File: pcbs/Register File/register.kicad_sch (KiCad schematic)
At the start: 20 parts, among them U201 74HCT574, U203 74HC245

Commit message: More sketching
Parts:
- added D108 (x3): Blue, LED_SMD:LED_0603_1608Metric, symbol Device:LED
- added R809 (x3): 4k7, Resistor_SMD:R_0603_1608Metric, symbol Device:R
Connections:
- net ~{A_{Enable}}: now reaches U203.19 (CE)
- net ~{A_{Enable}}: now also D108.1 (K)
- net ~{B_{Enable}}: now reaches U203.19 (CE)
- net ~{B_{Enable}}: now also D108.1 (K)
- net ~{C_{Enable}}: now reaches U203.19 (CE)
- net ~{C_{Enable}}: now also D108.1 (K)
- new net: D108.2 (A), R809.1 (x3)
- new net +5V: R809.2, R809.2, R809.2

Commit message: More connecting
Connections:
- net GND: now also U201.1 (OE)
- net r1: now also D802.2 (A)
- net r2: now also D803.2 (A)
- net r3: now also D804.2 (A)
- net r4: now also D805.2 (A)
- net r5: now also D806.2 (A)
- net r6: now also D807.2 (A)
- net C_{write}: now reaches U201.11 (Cp)
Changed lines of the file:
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@@
+    (stroke (width 0) (type default))
+  )
+  (wire (pts (xy 43.18 124.46) (xy 50.8 124.46))
     (stroke (width 0) (type default))
   )
@@
     (stroke (width 0) (type default))
   )
+  (wire (pts (xy 43.18 114.3) (xy 50.8 114.3))
+    (stroke (width 0) (type default))
+  )
   (wire (pts (xy 208.28 85.09) (xy 226.06 85.09))
     (stroke (width 0) (type default))
@@
     (stroke (width 0) (type default))
   )
+  (wire (pts (xy 50.8 55.88) (xy 64.77 55.88))
+    (stroke (width 0) (type default))
+  )
+  (wire (pts (xy 43.18 104.14) (xy 50.8 104.14))
+    (stroke (width 0) (type default))
+  )
   (bus (pts (xy 228.6 92.71) (xy 228.6 95.25))
     (stroke (width 0) (type default))
@@
     (stroke (width 0) (type default))
   )
+  (wire (pts (xy 43.18 134.62) (xy 50.8 134.62))
+    (stroke (width 0) (type default))
+  )
   (bus (pts (xy 228.6 87.63) (xy 228.6 90.17))
     (stroke (width 0) (type default))
@@
     (stroke (width 0) (type default))
   )
+  (wire (pts (xy 64.77 58.42) (xy 60.96 58.42))
+    (stroke (width 0) (type default))
+  )
   (bus (pts (xy 228.6 132.08) (xy 228.6 134.62))
     (stroke (width 0) (type default))
@@
     (stroke (width 0) (type default))
   )
+  (wire (pts (xy 43.18 144.78) (xy 50.8 144.78))
+    (stroke (width 0) (type default))
+  )
   (wire (pts (xy 208.28 33.02) (xy 226.06 33.02))
     (stroke (width 0) (type default))
@@
     (stroke (width 0) (type default))
   )
+  (wire (pts (xy 43.18 154.94) (xy 50.8 154.94))
+    (stroke (width 0) (type default))
+  )
   (wire (pts (xy 182.88 127) (xy 120.65 127))
     (stroke (width 0) (type default))
   )
+  (wire (pts (xy 60.96 58.42) (xy 60.96 60.96))
+    (stroke (width 0) (type default))
+  )
   (bus (pts (xy 228.6 142.24) (xy 228.6 144.78))
     (stroke (width 0) (type default))
@@
     (effects (font (size 1.27 1.27)) (justify left bottom))
   )
+  (label "r1" (at 43.18 104.14 0) (fields_autoplaced)
+    (effects (font (size 1.27 1.27)) (justify left bottom))
+  )
+  (label "r5" (at 43.18 144.78 0) (fields_autoplaced)
+    (effects (font (size 1.27 1.27)) (justify left bottom))
+  )
+  (label "r2" (at 43.18 114.3 0) (fields_autoplaced)
+    (effects (font (size 1.27 1.27)) (justify left bottom))
+  )
   (label "C7" (at 50.8 50.8 0) (fields_autoplaced)
     (effects (font (size 1.27 1.27)) (justify left bottom))
@@
     (effects (font (size 1.27 1.27)) (justify left bottom))
   )
+  (label "r3" (at 43.18 124.46 0) (fields_autoplaced)
+    (effects (font (size 1.27 1.27)) (justify left bottom))
+  )
   (label "r5" (at 99.06 45.72 0) (fields_autoplaced)
     (effects (font (size 1.27 1.27)) (justify left bottom))
@@
     (effects (font (size 1.27 1.27)) (justify left bottom))
   )
+  (label "r6" (at 43.18 154.94 0) (fields_autoplaced)
+    (effects (font (size 1.27 1.27)) (justify left bottom))
+  )
   (label "B2" (at 208.28 85.09 0) (fields_autoplaced)
     (effects (font (size 1.27 1.27)) (justify left bottom))
@@
   )
   (label "r0" (at 43.18 93.98 0) (fields_autoplaced)
+    (effects (font (size 1.27 1.27)) (justify left bottom))
+  )
+  (label "r4" (at 43.18 134.62 0) (fields_autoplaced)
     (effects (font (size 1.27 1.27)) (justify left bottom))
   )
@@
   (hierarchical_label "B[0..7]" (shape output) (at 247.65 72.39 0) (fields_autoplaced)
     (effects (font (size 1.27 1.27)) (justify left))
+  )
+  (hierarchical_label "C_{write}" (shape input) (at 50.8 55.88 180) (fields_autoplaced)
+    (effects (font (size 1.27 1.27)) (justify right))
   )
   (symbol (lib_id "Device:R") (at 166.37 116.84 270) (unit 1)
@@
         )
       )
+    )
+  )
+  (symbol (lib_name "GND_1") (lib_id "power:GND") (at 60.96 60.96 0) (unit 1)
+    (in_bom yes) (on_board yes) (dnp no) (fields_autoplaced)
+    (property "Reference" "#PWR0205" (at 60.96 67.31 0)
+      (effects (font (size 1.27 1.27)) hide)
+    )
+    (property "Value" "GND" (at 60.96 66.04 0)
+      (effects (font (size 1.27 1.27)))
+    )
+    (property "Footprint" "" (at 60.96 60.96 0)
+      (effects (font (size 1.27 1.27)) hide)
+    )
+    (property "Datasheet" "" (at 60.96 60.96 0)
+      (effects (font (size 1.27 1.27)) hide)
+    )
+    (pin "1")
+    (instances
+      (project "Register File"
+        (path "/9748b4de-07f7-464d-8b11-64fc866bac4c/9394d714-1820-477b-aab0-a9d71bb5ee5c"
+          (reference "#PWR0205") (unit 1)
+        )
+        (path "/9748b4de-07f7-464d-8b11-64fc866bac4c/834893a6-a9c4-4230-b12d-8490f053213e"
+          (reference "#PWR0305") (unit 1)
+        )
+        (path "/9748b4de-07f7-464d-8b11-64fc866bac4c/4dbf28be-5b5c-4207-8488-535f1c399bc6"
+          (reference "#PWR0405") (unit 1)
+        )
+        (path "/9748b4de-07f7-464d-8b11-64fc866bac4c/cb795ff7-ba35-4df7-ae01-85f6e0183a53"
+          (reference "#PWR0505") (unit 1)
+        )
+        (path "/9748b4de-07f7-464d-8b11-64fc866bac4c/c5b4a55a-958e-4012-8139-b0afd70d67a1"
+          (reference "#PWR0605") (unit 1)
+        )
+        (path "/9748b4de-07f7-464d-8b11-64fc866bac4c/a37b855b-764b-47a1-be98-45e29ef72f3b"
+          (reference "#PWR0705") (unit 1)
+        )
+        (path "/9748b4de-07f7-464d-8b11-64fc866bac4c/b38b4b23-22e0-4015-98d9-f235dafba938"
+          (reference "#PWR0805") (unit 1)
+        )
+        (path "/9748b4de-07f7-464d-8b11-64fc866bac4c/5f8f38cf-62d2-470f-8060-72fd5c305ae9"
+          (reference "#PWR0905") (unit 1)
+        )
+      )

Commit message: More work
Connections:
- net +5V: now also U201.20 (VCC), U203.20 (VCC), U203.20 (VCC), U203.20 (VCC)
- net GND: now also U201.10 (GND), U203.10 (GND), U203.10 (GND), U203.10 (GND)

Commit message: Remember the control buses...
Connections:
- net +5V: now also U203.1 (A->B), U203.1 (A->B), U203.1 (A->B)
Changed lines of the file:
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@@
+    (stroke (width 0) (type default))
+  )
+  (wire (pts (xy 176.53 149.86) (xy 182.88 149.86))
     (stroke (width 0) (type default))
   )
@@
     (stroke (width 0) (type default))
   )
+  (wire (pts (xy 176.53 102.87) (xy 182.88 102.87))
+    (stroke (width 0) (type default))
+  )
   (wire (pts (xy 208.28 87.63) (xy 226.06 87.63))
     (stroke (width 0) (type default))
@@
   )
   (wire (pts (xy 76.2 154.94) (xy 76.2 144.78))
+    (stroke (width 0) (type default))
+  )
+  (wire (pts (xy 176.53 55.88) (xy 182.88 55.88))
     (stroke (width 0) (type default))
   )
@@
     )
   )
+  (symbol (lib_id "power:+5V") (at 176.53 102.87 90) (unit 1)
+    (in_bom yes) (on_board yes) (dnp no) (fields_autoplaced)
+    (property "Reference" "#PWR0315" (at 180.34 102.87 0)
+      (effects (font (size 1.27 1.27)) hide)
+    )
+    (property "Value" "+5V" (at 172.72 102.87 90)
+      (effects (font (size 1.27 1.27)) (justify left))
+    )
+    (property "Footprint" "" (at 176.53 102.87 0)
+      (effects (font (size 1.27 1.27)) hide)
+    )
+    (property "Datasheet" "" (at 176.53 102.87 0)
+      (effects (font (size 1.27 1.27)) hide)
+    )
+    (pin "1")
+    (instances
+      (project "Register File"
+        (path "/9748b4de-07f7-464d-8b11-64fc866bac4c/834893a6-a9c4-4230-b12d-8490f053213e"
+          (reference "#PWR0315") (unit 1)
+        )
+        (path "/9748b4de-07f7-464d-8b11-64fc866bac4c/9394d714-1820-477b-aab0-a9d71bb5ee5c"
+          (reference "#PWR0215") (unit 1)
+        )
+        (path "/9748b4de-07f7-464d-8b11-64fc866bac4c/4dbf28be-5b5c-4207-8488-535f1c399bc6"
+          (reference "#PWR0415") (unit 1)
+        )
+        (path "/9748b4de-07f7-464d-8b11-64fc866bac4c/cb795ff7-ba35-4df7-ae01-85f6e0183a53"
+          (reference "#PWR0515") (unit 1)
+        )
+        (path "/9748b4de-07f7-464d-8b11-64fc866bac4c/c5b4a55a-958e-4012-8139-b0afd70d67a1"
+          (reference "#PWR0615") (unit 1)
+        )
+        (path "/9748b4de-07f7-464d-8b11-64fc866bac4c/a37b855b-764b-47a1-be98-45e29ef72f3b"
+          (reference "#PWR0715") (unit 1)
+        )
+        (path "/9748b4de-07f7-464d-8b11-64fc866bac4c/b38b4b23-22e0-4015-98d9-f235dafba938"
+          (reference "#PWR0815") (unit 1)
+        )
+        (path "/9748b4de-07f7-464d-8b11-64fc866bac4c/5f8f38cf-62d2-470f-8060-72fd5c305ae9"
+          (reference "#PWR0915") (unit 1)
+        )
+      )
+    )
+  )
   (symbol (lib_id "Device:LED") (at 54.61 144.78 180) (unit 1)
     (in_bom yes) (on_board yes) (dnp no) (fields_autoplaced)
@@
         (path "/9748b4de-07f7-464d-8b11-64fc866bac4c/5f8f38cf-62d2-470f-8060-72fd5c305ae9"
           (reference "R906") (unit 1)
+        )
+      )
+    )
+  )
+  (symbol (lib_id "power:+5V") (at 176.53 149.86 90) (unit 1)
+    (in_bom yes) (on_board yes) (dnp no) (fields_autoplaced)
+    (property "Reference" "#PWR0316" (at 180.34 149.86 0)
+      (effects (font (size 1.27 1.27)) hide)
+    )
+    (property "Value" "+5V" (at 172.72 149.86 90)
+      (effects (font (size 1.27 1.27)) (justify left))
+    )
+    (property "Footprint" "" (at 176.53 149.86 0)
+      (effects (font (size 1.27 1.27)) hide)
+    )
+    (property "Datasheet" "" (at 176.53 149.86 0)
+      (effects (font (size 1.27 1.27)) hide)
+    )
+    (pin "1")
+    (instances
+      (project "Register File"
+        (path "/9748b4de-07f7-464d-8b11-64fc866bac4c/834893a6-a9c4-4230-b12d-8490f053213e"
+          (reference "#PWR0316") (unit 1)
+        )
+        (path "/9748b4de-07f7-464d-8b11-64fc866bac4c/9394d714-1820-477b-aab0-a9d71bb5ee5c"
+          (reference "#PWR0216") (unit 1)
+        )
+        (path "/9748b4de-07f7-464d-8b11-64fc866bac4c/4dbf28be-5b5c-4207-8488-535f1c399bc6"
+          (reference "#PWR0416") (unit 1)
+        )
+        (path "/9748b4de-07f7-464d-8b11-64fc866bac4c/cb795ff7-ba35-4df7-ae01-85f6e0183a53"
+          (reference "#PWR0516") (unit 1)
+        )
+        (path "/9748b4de-07f7-464d-8b11-64fc866bac4c/c5b4a55a-958e-4012-8139-b0afd70d67a1"
+          (reference "#PWR0616") (unit 1)
+        )
+        (path "/9748b4de-07f7-464d-8b11-64fc866bac4c/a37b855b-764b-47a1-be98-45e29ef72f3b"
+          (reference "#PWR0716") (unit 1)
+        )
+        (path "/9748b4de-07f7-464d-8b11-64fc866bac4c/b38b4b23-22e0-4015-98d9-f235dafba938"
+          (reference "#PWR0816") (unit 1)
+        )
+        (path "/9748b4de-07f7-464d-8b11-64fc866bac4c/5f8f38cf-62d2-470f-8060-72fd5c305ae9"
+          (reference "#PWR0916") (unit 1)
         )
       )
@@
         )
       )
+    )
+  )
+  (symbol (lib_id "power:+5V") (at 176.53 55.88 90) (unit 1)
+    (in_bom yes) (on_board yes) (dnp no) (fields_autoplaced)
+    (property "Reference" "#PWR0314" (at 180.34 55.88 0)
+      (effects (font (size 1.27 1.27)) hide)
+    )
+    (property "Value" "+5V" (at 172.72 55.88 90)
+      (effects (font (size 1.27 1.27)) (justify left))
+    )
+    (property "Footprint" "" (at 176.53 55.88 0)
+      (effects (font (size 1.27 1.27)) hide)
+    )
+    (property "Datasheet" "" (at 176.53 55.88 0)
+      (effects (font (size 1.27 1.27)) hide)
+    )
+    (pin "1")
+    (instances
+      (project "Register File"
+        (path "/9748b4de-07f7-464d-8b11-64fc866bac4c/834893a6-a9c4-4230-b12d-8490f053213e"
+          (reference "#PWR0314") (unit 1)
+        )
+        (path "/9748b4de-07f7-464d-8b11-64fc866bac4c/9394d714-1820-477b-aab0-a9d71bb5ee5c"
+          (reference "#PWR0214") (unit 1)
+        )
+        (path "/9748b4de-07f7-464d-8b11-64fc866bac4c/4dbf28be-5b5c-4207-8488-535f1c399bc6"
+          (reference "#PWR0414") (unit 1)
+        )
+        (path "/9748b4de-07f7-464d-8b11-64fc866bac4c/cb795ff7-ba35-4df7-ae01-85f6e0183a53"
+          (reference "#PWR0514") (unit 1)
+        )
+        (path "/9748b4de-07f7-464d-8b11-64fc866bac4c/c5b4a55a-958e-4012-8139-b0afd70d67a1"
+          (reference "#PWR0614") (unit 1)
+        )
+        (path "/9748b4de-07f7-464d-8b11-64fc866bac4c/a37b855b-764b-47a1-be98-45e29ef72f3b"
+          (reference "#PWR0714") (unit 1)
+        )
+        (path "/9748b4de-07f7-464d-8b11-64fc866bac4c/b38b4b23-22e0-4015-98d9-f235dafba938"
+          (reference "#PWR0814") (unit 1)
+        )
+        (path "/9748b4de-07f7-464d-8b11-64fc866bac4c/5f8f38cf-62d2-470f-8060-72fd5c305ae9"
+          (reference "#PWR0914") (unit 1)
+        )
+      )

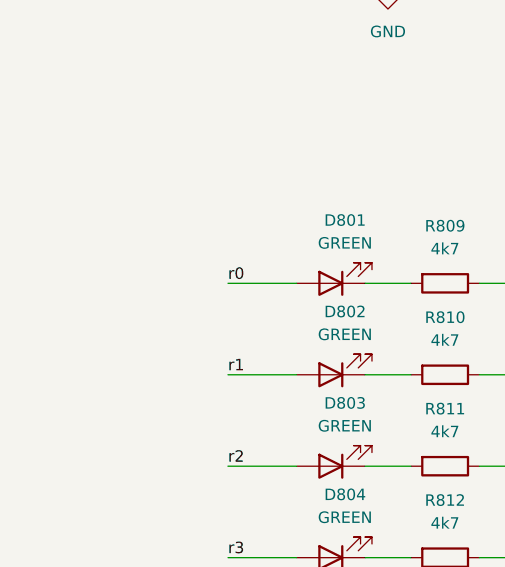
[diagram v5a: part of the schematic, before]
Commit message: Adding some capacitors
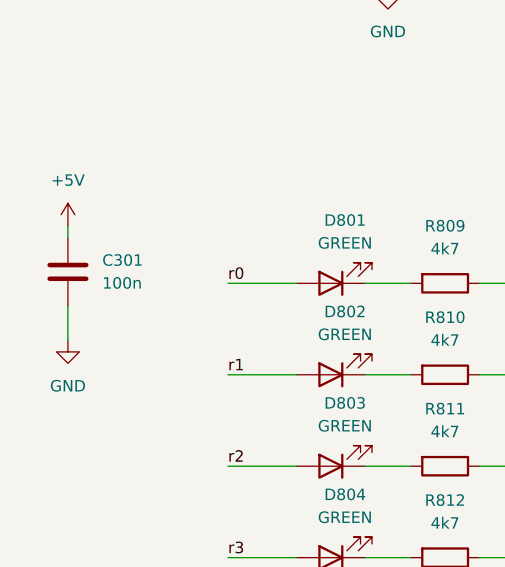
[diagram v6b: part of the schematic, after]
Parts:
- added C301: 100n, Capacitor_SMD:C_0603_1608Metric, symbol Device:C
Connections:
- net +5V: now also C301.1
- net GND: now also C301.2
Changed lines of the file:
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@@
+    (stroke (width 0) (type default))
+  )
+  (wire (pts (xy 25.4 88.9) (xy 25.4 87.63))
     (stroke (width 0) (type default))
   )
@@
   )
   (wire (pts (xy 43.18 124.46) (xy 50.8 124.46))
+    (stroke (width 0) (type default))
+  )
+  (wire (pts (xy 25.4 96.52) (xy 25.4 100.33))
     (stroke (width 0) (type default))
   )
@@
     )
   )
+  (symbol (lib_id "Device:C") (at 25.4 92.71 0) (unit 1)
+    (in_bom yes) (on_board yes) (dnp no) (fields_autoplaced)
+    (property "Reference" "C301" (at 29.21 91.4399 0)
+      (effects (font (size 1.27 1.27)) (justify left))
+    )
+    (property "Value" "100n" (at 29.21 93.9799 0)
+      (effects (font (size 1.27 1.27)) (justify left))
+    )
+    (property "Footprint" "Capacitor_SMD:C_0603_1608Metric" (at 26.3652 96.52 0)
+      (effects (font (size 1.27 1.27)) hide)
+    )
+    (property "Datasheet" "https://datasheet.lcsc.com/lcsc/1809301912_YAGEO-CC0603KRX7R9BB104_C14663.pdf" (at 25.4 92.71 0)
+      (effects (font (size 1.27 1.27)) hide)
+    )
+    (property "LCSC" "C14663" (at 25.4 92.71 0)
+      (effects (font (size 1.27 1.27)) hide)
+    )
+    (pin "1")
+    (pin "2")
+    (instances
+      (project "SALU"
+        (path "/214bf021-2aca-4e47-860d-c4f395ab302b/8ff9c7f7-723f-421c-b21d-a9beb8766b95"
+          (reference "C301") (unit 1)
+        )
+      )
+      (project "Register File"
+        (path "/9748b4de-07f7-464d-8b11-64fc866bac4c/9394d714-1820-477b-aab0-a9d71bb5ee5c"
+          (reference "C201") (unit 1)
+        )
+        (path "/9748b4de-07f7-464d-8b11-64fc866bac4c/834893a6-a9c4-4230-b12d-8490f053213e"
+          (reference "C301") (unit 1)
+        )
+        (path "/9748b4de-07f7-464d-8b11-64fc866bac4c/4dbf28be-5b5c-4207-8488-535f1c399bc6"
+          (reference "C401") (unit 1)
+        )
+        (path "/9748b4de-07f7-464d-8b11-64fc866bac4c/cb795ff7-ba35-4df7-ae01-85f6e0183a53"
+          (reference "C501") (unit 1)
+        )
+        (path "/9748b4de-07f7-464d-8b11-64fc866bac4c/c5b4a55a-958e-4012-8139-b0afd70d67a1"
+          (reference "C601") (unit 1)
+        )
+        (path "/9748b4de-07f7-464d-8b11-64fc866bac4c/a37b855b-764b-47a1-be98-45e29ef72f3b"
+          (reference "C701") (unit 1)
+        )
+        (path "/9748b4de-07f7-464d-8b11-64fc866bac4c/b38b4b23-22e0-4015-98d9-f235dafba938"
+          (reference "C801") (unit 1)
+        )
+        (path "/9748b4de-07f7-464d-8b11-64fc866bac4c/5f8f38cf-62d2-470f-8060-72fd5c305ae9"
+          (reference "C901") (unit 1)
+        )
+      )
+    )
+  )
   (symbol (lib_id "power:+5V") (at 193.04 118.11 90) (unit 1)
     (in_bom yes) (on_board yes) (dnp no) (fields_autoplaced)
@@
         (path "/9748b4de-07f7-464d-8b11-64fc866bac4c/5f8f38cf-62d2-470f-8060-72fd5c305ae9"
           (reference "#PWR0915") (unit 1)
+        )
+      )
+    )
+  )
+  (symbol (lib_id "power:GND") (at 25.4 100.33 0) (unit 1)
+    (in_bom yes) (on_board yes) (dnp no) (fields_autoplaced)
+    (property "Reference" "#PWR0302" (at 25.4 106.68 0)
+      (effects (font (size 1.27 1.27)) hide)
+    )
+    (property "Value" "GND" (at 25.4 105.41 0)
+      (effects (font (size 1.27 1.27)))
+    )
+    (property "Footprint" "" (at 25.4 100.33 0)
+      (effects (font (size 1.27 1.27)) hide)
+    )
+    (property "Datasheet" "" (at 25.4 100.33 0)
+      (effects (font (size 1.27 1.27)) hide)
+    )
+    (pin "1")
+    (instances
+      (project "SALU"
+        (path "/214bf021-2aca-4e47-860d-c4f395ab302b/8ff9c7f7-723f-421c-b21d-a9beb8766b95"
+          (reference "#PWR0302") (unit 1)
+        )
+      )
+      (project "Register File"
+        (path "/9748b4de-07f7-464d-8b11-64fc866bac4c/9394d714-1820-477b-aab0-a9d71bb5ee5c"
+          (reference "#PWR0218") (unit 1)
+        )
+        (path "/9748b4de-07f7-464d-8b11-64fc866bac4c/834893a6-a9c4-4230-b12d-8490f053213e"
+          (reference "#PWR0318") (unit 1)
+        )
+        (path "/9748b4de-07f7-464d-8b11-64fc866bac4c/4dbf28be-5b5c-4207-8488-535f1c399bc6"
+          (reference "#PWR0418") (unit 1)
+        )
+        (path "/9748b4de-07f7-464d-8b11-64fc866bac4c/cb795ff7-ba35-4df7-ae01-85f6e0183a53"
+          (reference "#PWR0518") (unit 1)
+        )
+        (path "/9748b4de-07f7-464d-8b11-64fc866bac4c/c5b4a55a-958e-4012-8139-b0afd70d67a1"
+          (reference "#PWR0618") (unit 1)
+        )
+        (path "/9748b4de-07f7-464d-8b11-64fc866bac4c/a37b855b-764b-47a1-be98-45e29ef72f3b"
+          (reference "#PWR0718") (unit 1)
+        )
+        (path "/9748b4de-07f7-464d-8b11-64fc866bac4c/b38b4b23-22e0-4015-98d9-f235dafba938"
+          (reference "#PWR0818") (unit 1)
+        )
+        (path "/9748b4de-07f7-464d-8b11-64fc866bac4c/5f8f38cf-62d2-470f-8060-72fd5c305ae9"
+          (reference "#PWR0918") (unit 1)
         )
       )
@@
         )
       )
+    )
+  )
+  (symbol (lib_id "power:+5V") (at 25.4 87.63 0) (unit 1)
+    (in_bom yes) (on_board yes) (dnp no) (fields_autoplaced)
+    (property "Reference" "#PWR0301" (at 25.4 91.44 0)
+      (effects (font (size 1.27 1.27)) hide)
+    )
+    (property "Value" "+5V" (at 25.4 82.55 0)
+      (effects (font (size 1.27 1.27)))
+    )
+    (property "Footprint" "" (at 25.4 87.63 0)
+      (effects (font (size 1.27 1.27)) hide)
+    )
+    (property "Datasheet" "" (at 25.4 87.63 0)
+      (effects (font (size 1.27 1.27)) hide)
+    )
+    (pin "1")
+    (instances
+      (project "SALU"
+        (path "/214bf021-2aca-4e47-860d-c4f395ab302b/8ff9c7f7-723f-421c-b21d-a9beb8766b95"
+          (reference "#PWR0301") (unit 1)
+        )
+      )
+      (project "Register File"
+        (path "/9748b4de-07f7-464d-8b11-64fc866bac4c/9394d714-1820-477b-aab0-a9d71bb5ee5c"
+          (reference "#PWR0217") (unit 1)
+        )
+        (path "/9748b4de-07f7-464d-8b11-64fc866bac4c/834893a6-a9c4-4230-b12d-8490f053213e"
+          (reference "#PWR0317") (unit 1)
+        )
+        (path "/9748b4de-07f7-464d-8b11-64fc866bac4c/4dbf28be-5b5c-4207-8488-535f1c399bc6"
+          (reference "#PWR0417") (unit 1)
+        )
+        (path "/9748b4de-07f7-464d-8b11-64fc866bac4c/cb795ff7-ba35-4df7-ae01-85f6e0183a53"
+          (reference "#PWR0517") (unit 1)
+        )
+        (path "/9748b4de-07f7-464d-8b11-64fc866bac4c/c5b4a55a-958e-4012-8139-b0afd70d67a1"
+          (reference "#PWR0617") (unit 1)
+        )
+        (path "/9748b4de-07f7-464d-8b11-64fc866bac4c/a37b855b-764b-47a1-be98-45e29ef72f3b"
+          (reference "#PWR0717") (unit 1)
+        )
+        (path "/9748b4de-07f7-464d-8b11-64fc866bac4c/b38b4b23-22e0-4015-98d9-f235dafba938"
+          (reference "#PWR0817") (unit 1)
+        )
+        (path "/9748b4de-07f7-464d-8b11-64fc866bac4c/5f8f38cf-62d2-470f-8060-72fd5c305ae9"
+          (reference "#PWR0917") (unit 1)
+        )
+      )
